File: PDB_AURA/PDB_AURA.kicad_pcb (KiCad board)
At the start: 4 copper layers, 50 x 50 mm, 84 parts, among them J100 XT30PW-M, J300 XT30PW-F, J301 XT30PW-F, J302 532617012, J303 XT30PW-F, J304 XT30PW-F, Q100 CSD18540Q5B, Q200 CSD18540Q5B, Q201 CSD18510Q5B, Q300 HSK10N06, Q301 HSK10N06, U100 LM74700, U200 LM25145RGYR, U300 LTV-217-B-G, U301 LTV-217-B-G, U302 INA219AIDCNR

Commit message: Continued Routing
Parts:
- C218: moved to F.Cu
- moved D300 29.0 mm to (60.5, 58.0)
- moved D301 29.0 mm to (89.5, 58.0)
- moved TP200 10.5 mm to (91.0, 79.0)
- moved C218 7.16 mm to (97.5, 62.5), turned to 90 degrees
- moved JP100 1.80 mm to (68.2, 79.0)
- moved R301 1.58 mm to (63.2, 65.0), turned to 180 degrees
- moved R307 1.58 mm to (86.8, 65.0), turned to 0 degrees
- moved TP201 0.15 mm to (70.0, 68.3)
- turned U300 to 90 degrees
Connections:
- J100 pad 4: GND -> +BATT
- J302 pad 1: +5V -> GND
- J302 pad 10: GND -> +5V
- J302 pad 11: GND -> +5V
- J302 pad 12: GND -> +5V
- J302 pad 2: +5V -> GND
- J302 pad 3: +5V -> GND
- J302 pad 5: SCL -> SDA
- J302 pad 6: SDA -> SCL
- J303 pad 3: GND -> +BATT_FILT
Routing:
- net GND: track 0.00 -> 21.4 mm, vias 162 -> 180
- net SDA: track 0.00 -> 19.5 mm
- net SCL: track 0.00 -> 19.2 mm
- net /200_Buck_Regulator/5V_HO: track 0.00 -> 19.1 mm, vias 0 -> 2
- net +5V_VCC: track 0.00 -> 17.8 mm, vias 0 -> 3
- net MSFT_2: track 0.00 -> 17.5 mm
- net /300_Connectors/VGS_CH1: track 0.00 -> 13.9 mm, vias 0 -> 2
- net /200_Buck_Regulator/COMP_FB_C: track 0.00 -> 13.5 mm, vias 0 -> 2
- net MSFT_1: track 0.00 -> 13.3 mm
- net /200_Buck_Regulator/5V_FB: track 0.00 -> 13.2 mm, vias 0 -> 1
- net /300_Connectors/MSFT_2_R: track 0.00 -> 13.0 mm, vias 0 -> 2
- net /300_Connectors/MSFT_1_R: track 0.00 -> 9.20 mm
- net /200_Buck_Regulator/5V_LO: track 0.00 -> 8.64 mm, vias 0 -> 2
- net /200_Buck_Regulator/5V_SW: track 0.00 -> 7.45 mm
- net +5V: track 0.00 -> 6.99 mm, vias 3 -> 5
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- added copper zone on B.Cu, net +5V
- added copper zone on B.Cu, net +BATT
- added copper zone on F.Cu, net +BATT
- added copper zone on In2.Cu, net +BATT_FILT
- added copper zone on F.Cu, net /300_Connectors/VBAT_CH1
- added copper zone on F.Cu, net /300_Connectors/VBAT_CH2
- added copper zone on B.Cu, net INA_IN+
- added copper zone on F.Cu, net INA_IN+

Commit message: First PDB Version
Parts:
- moved D200 2.03 mm to (96.5, 71.2)
- moved R211 2.03 mm to (93.9, 71.2)
- moved D100 1.75 mm to (96.5, 69.2)
- moved R101 1.72 mm to (93.9, 69.2)
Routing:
- net +5V: track 6.99 -> 72.5 mm, vias 5 -> 20
- net +3V3: track 0.00 -> 44.0 mm, vias 0 -> 2
- net MSFT_1: track 13.3 -> 47.0 mm, vias 0 -> 1
- net SCL: track 19.2 -> 38.2 mm, vias 0 -> 1
- net SDA: track 19.5 -> 37.0 mm, vias 0 -> 1
- net /300_Connectors/VGS_CH2: track 0.99 -> 14.4 mm
- net MSFT_2: track 17.5 -> 27.1 mm, vias 0 -> 1
- net /300_Connectors/VBAT_CH1: track 0.00 -> 6.71 mm, vias 2 -> 0
- net /200_Buck_Regulator/5V_SW: track 7.45 -> 13.6 mm, vias 12 -> 20
- net +BATT_FILT: track 5.73 -> 11.1 mm, vias 174 -> 181
- net GND: track 21.4 -> 23.9 mm, vias 180 -> 192
- net /200_Buck_Regulator/5V_HO: track 19.1 -> 20.3 mm
- net /200_Buck_Regulator/5V_LED: track 0.00 -> 1.28 mm
- net /100_Power/VBAT_LED: track 0.00 -> 1.28 mm
- net INA_IN+: vias 25 -> 33
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- added copper zone on B.Cu, net +BATT_FILT
- added copper zone on B.Cu, net /200_Buck_Regulator/5V_SW

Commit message: Second Iteration
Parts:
- C204, C205: value 22u -> 47u
- TP200, TP202: moved to F.Cu
- moved C205 13.4 mm to (89.5, 91.8)
- moved TP200 11.0 mm to (94.2, 89.5), turned to 0 degrees
- moved C216 3.50 mm to (95.5, 79.8)
- moved TP202 1.90 mm to (71.8, 74.2), turned to 0 degrees
- moved C210 1.00 mm to (74.8, 74.2)
- moved R210 1.00 mm to (75.8, 74.2)
- moved C300 0.50 mm to (73.3, 91.5)
- moved U302 0.50 mm to (75.8, 91.5)
- moved L200 0.25 mm to (85.2, 82.5), turned to -90 degrees
- moved TP203 0.10 mm to (70.0, 71.0)
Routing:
- net +5V: track 72.5 -> 83.1 mm, vias 20 -> 18
- net GND: track 23.9 -> 31.4 mm, vias 192 -> 253
- net +BATT: track 6.51 -> 0.00 mm, vias 49 -> 45
- net INA_IN+: track 3.58 -> 8.95 mm, vias 33 -> 38
- net +BATT_FILT: track 11.1 -> 14.2 mm, vias 181 -> 178
- net /200_Buck_Regulator/5V_PGOOD: track 4.44 -> 2.80 mm, vias 1 -> 0
- net /200_Buck_Regulator/5V_SW: track 13.6 -> 12.0 mm, vias 20 -> 9
- net MSFT_2: track 27.1 -> 28.6 mm
- net /300_Connectors/MSFT_2_R: track 13.0 -> 11.8 mm
- net SCL: track 38.2 -> 39.1 mm, vias 1 -> 3
- net SDA: track 37.0 -> 37.6 mm, vias 1 -> 3
- net /300_Connectors/VGS_CH2: track 14.4 -> 14.5 mm, vias 0 -> 2
- net +5V_VCC: track 17.8 -> 17.7 mm, vias 3 -> 2
- net +3V3: vias 2 -> 4

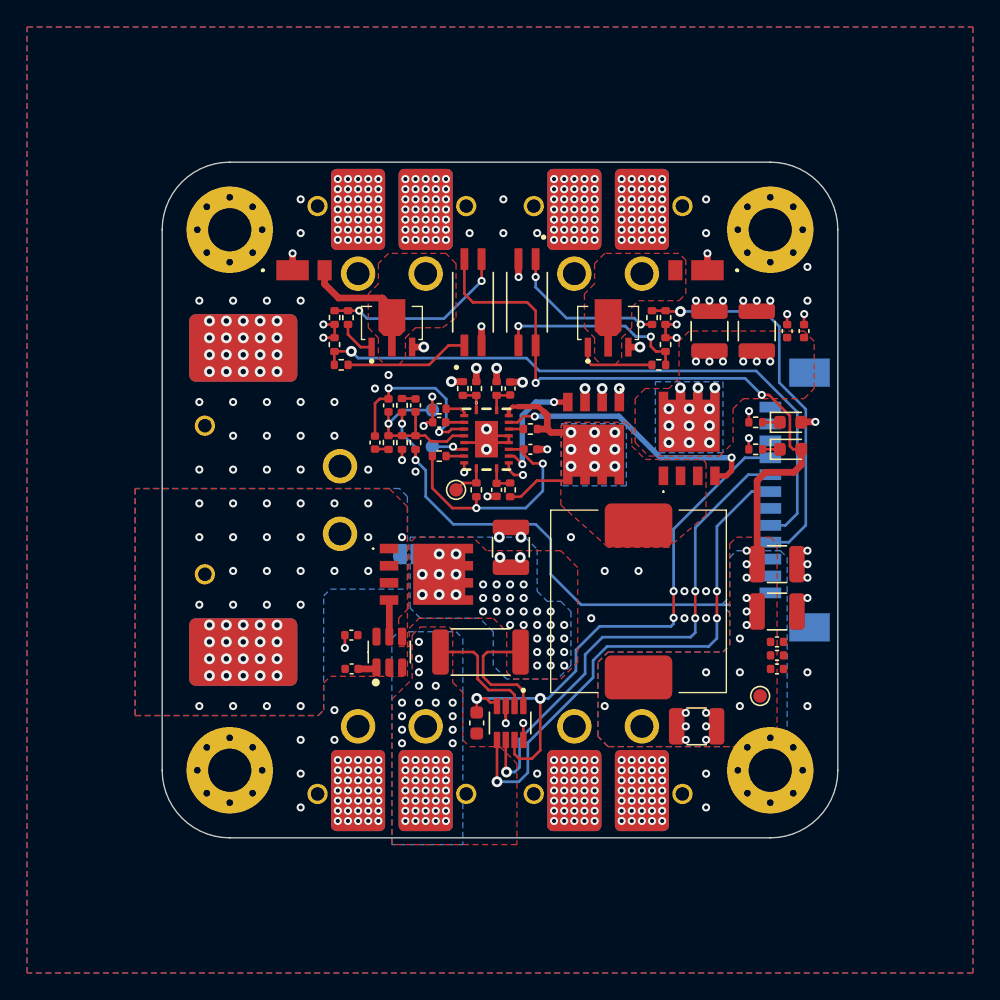
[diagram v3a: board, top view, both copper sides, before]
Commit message: Replaced JTAG with Flash
JTAG is used through USB so a Flash chip was added to MCU. PDB is just being cleaned up currently.
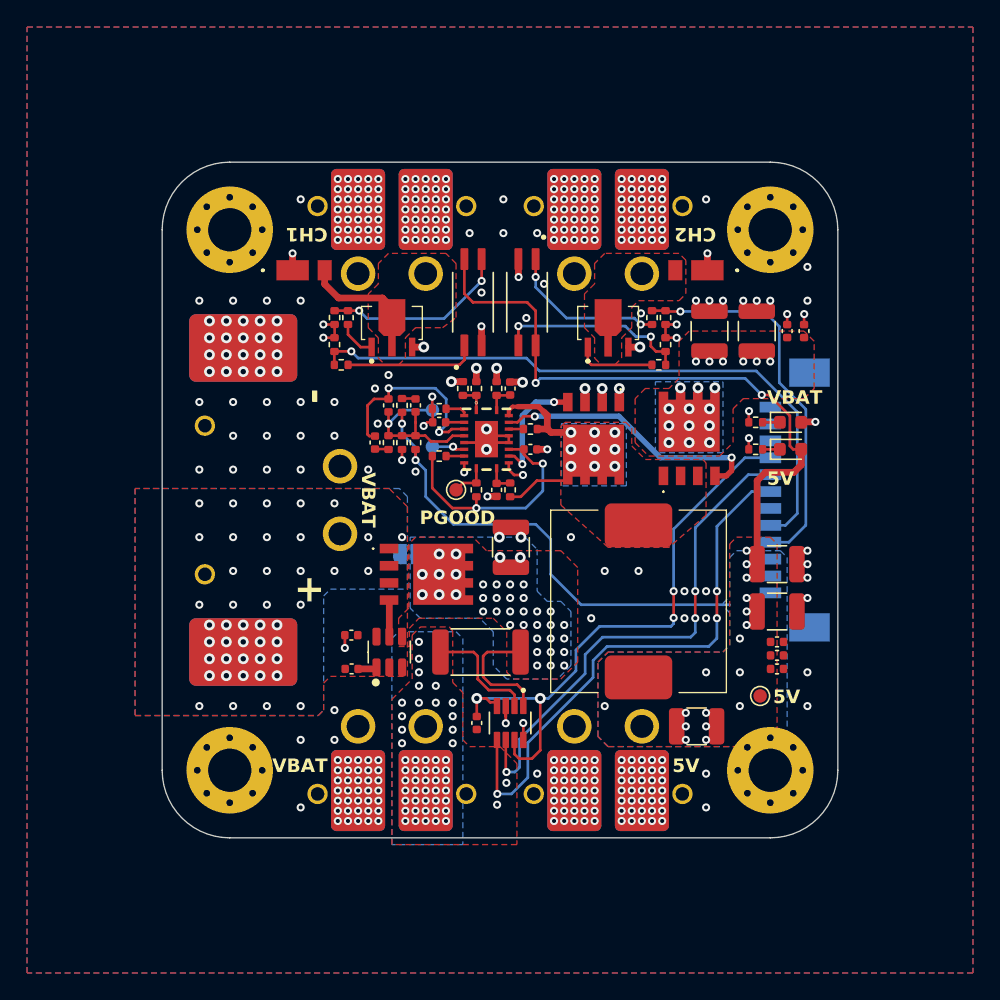
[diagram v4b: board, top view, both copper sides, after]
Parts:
- C300: footprint Capacitor_SMD:C_0603_1608Metric -> Capacitor_SMD:C_0402_1005Metric
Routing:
- net SCL: track 39.1 -> 40.6 mm
- net /200_Buck_Regulator/COMP_FB_C: track 13.5 -> 14.5 mm
- net /300_Connectors/MSFT_1_R: track 9.20 -> 9.83 mm
- net GND: vias 253 -> 257
- net +BATT: vias 45 -> 44
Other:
- board text added: "+"
- board text added: "-"
- board text added: "5V"
- board text added: "5V_FB"
- board text added: "CH1"
- board text added: "CH2"
- board text added: "PGOOD"
- board text added: "Power"
- board text added: "SYNC"
- board text added: "VBAT"

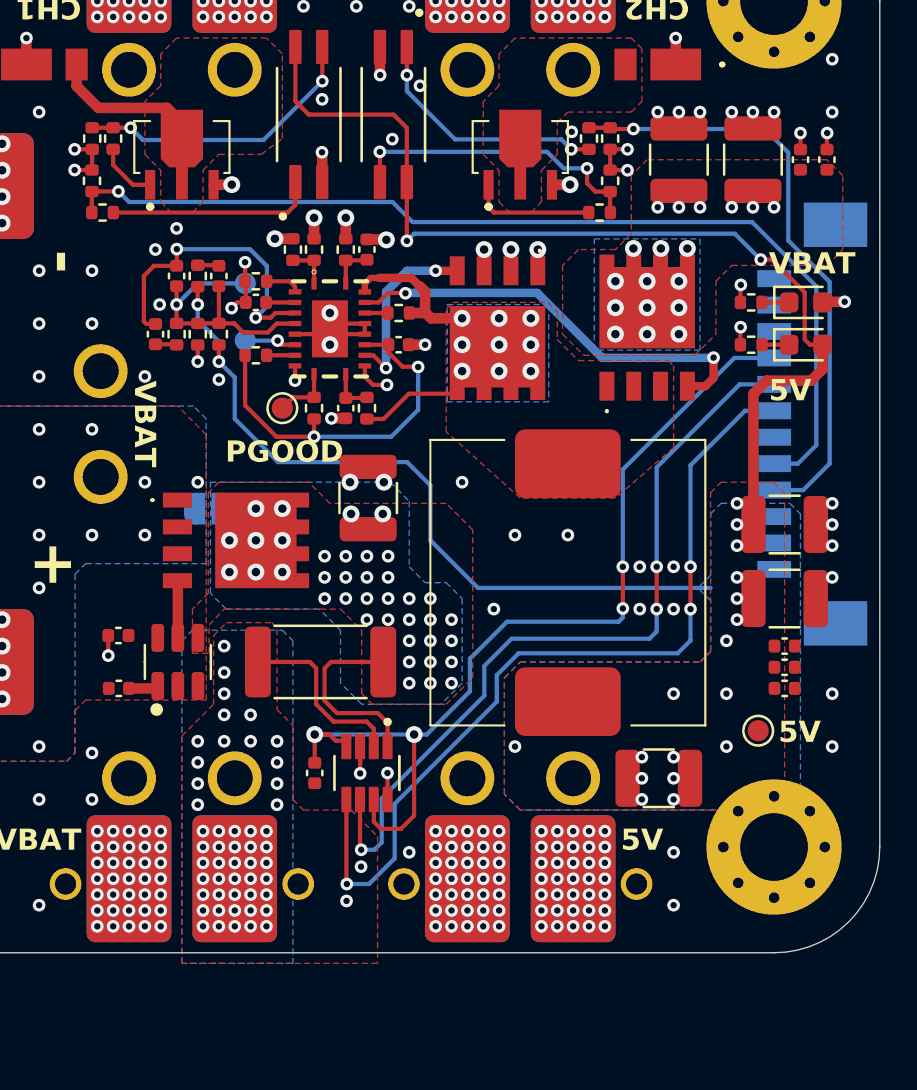
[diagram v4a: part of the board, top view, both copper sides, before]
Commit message: Fixed LM2514 Layout
Followed datasheet guidelines for the SW and HO traces.
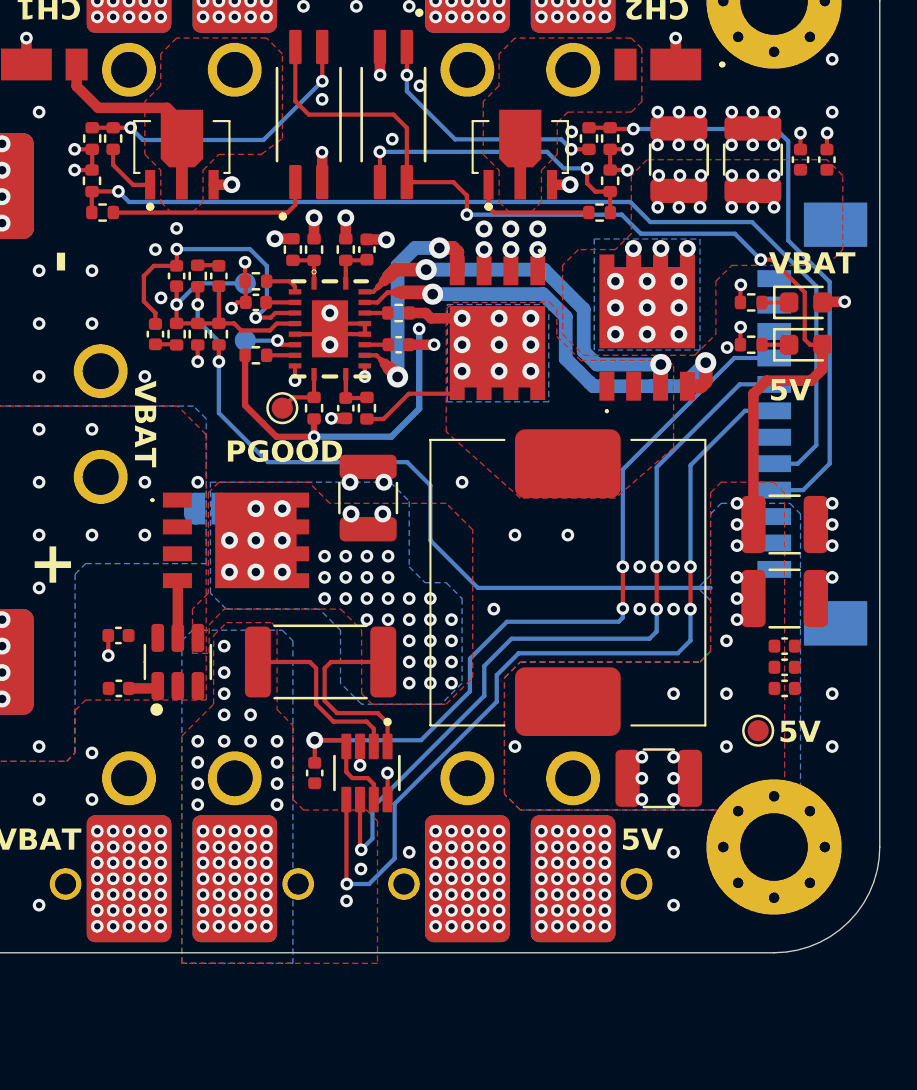
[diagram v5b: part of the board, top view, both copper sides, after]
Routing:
- net /200_Buck_Regulator/5V_SW: track 12.0 -> 26.0 mm, vias 9 -> 11
- net +3V3: track 44.0 -> 40.0 mm, vias 4 -> 3
- net /200_Buck_Regulator/5V_LO: track 8.63 -> 11.4 mm
- net /200_Buck_Regulator/5V_HO: track 20.3 -> 21.6 mm
- net +5V: track 83.1 -> 82.0 mm
- net GND: track 31.4 -> 30.4 mm, vias 257 -> 266
- net +BATT_FILT: vias 178 -> 184

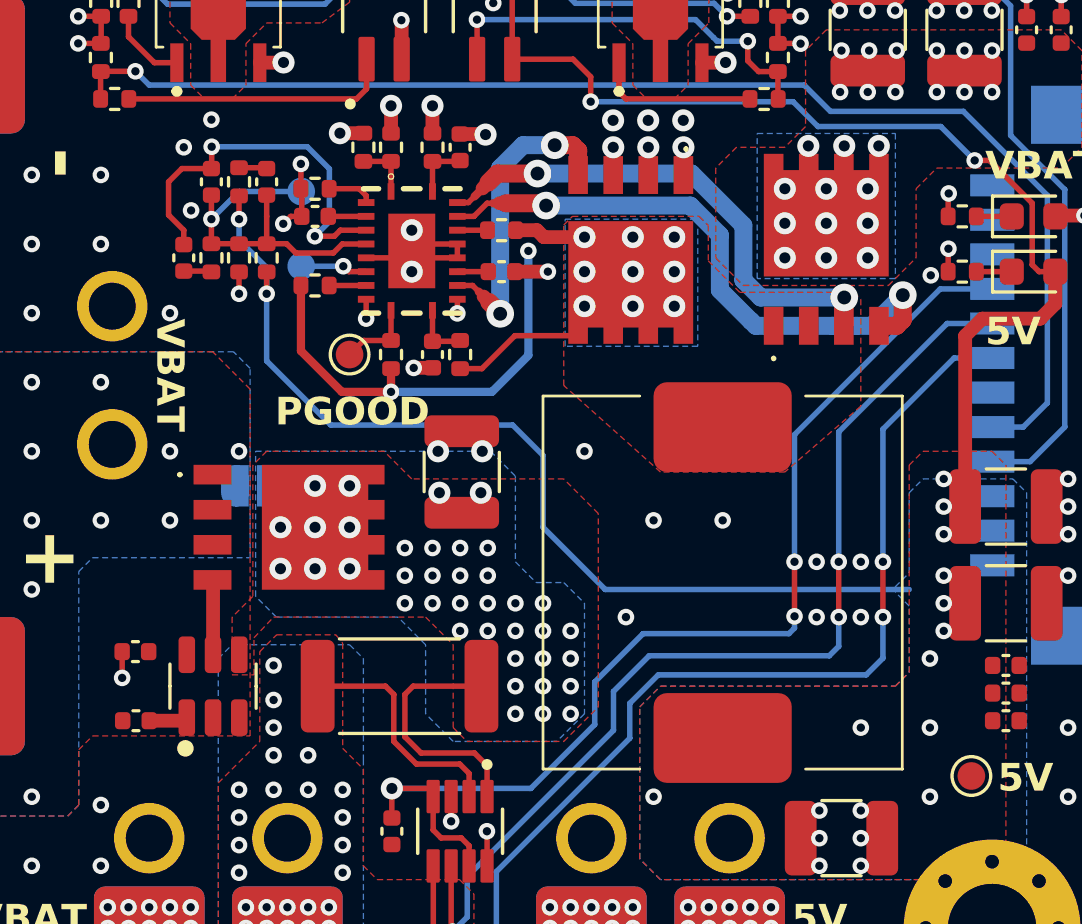
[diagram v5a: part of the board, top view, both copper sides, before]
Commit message: New Component Values
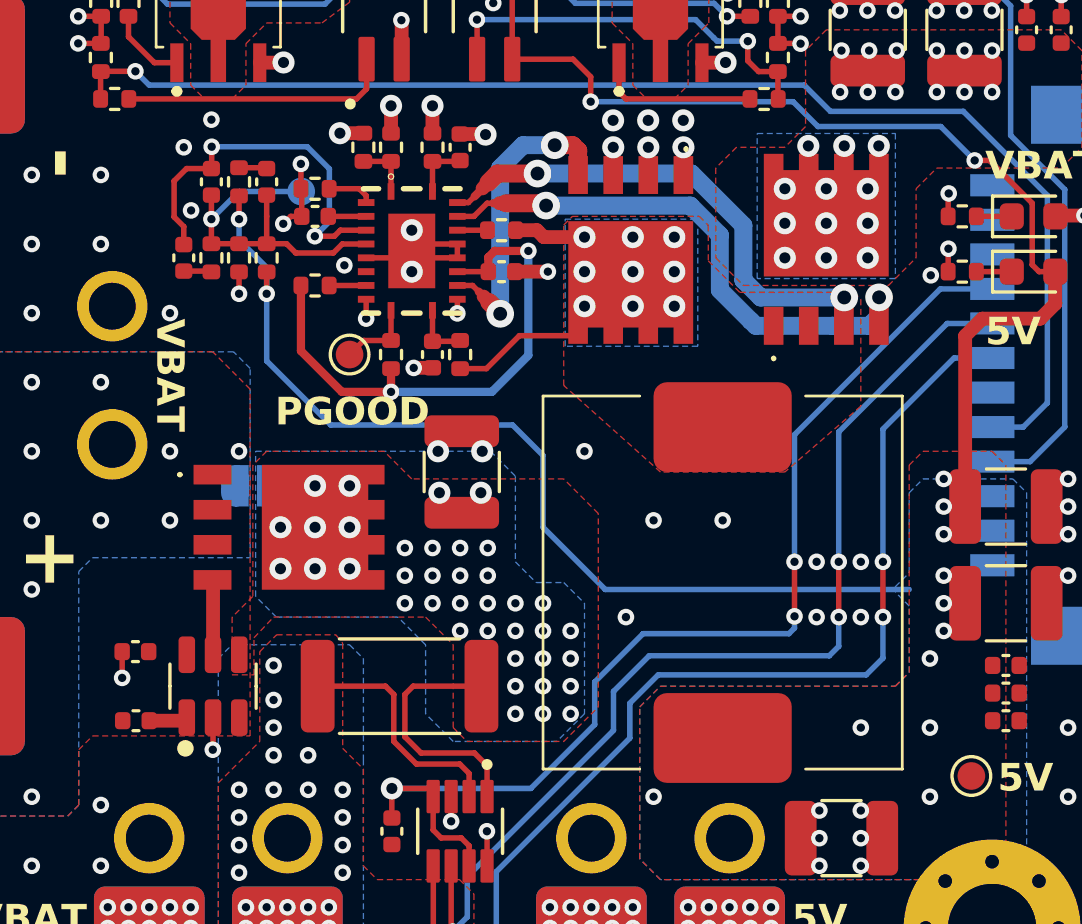
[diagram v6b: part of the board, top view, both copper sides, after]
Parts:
- removed TP203: TestPoint, TestPoint:TestPoint_Pad_D1.0mm
- C210: value 10p -> 27p
- C211: value 100n -> 47n
- C212: value 1n -> 2n2
- C213: value 8n2 -> 18n
- C214: value 390p -> 1n8
- R200: value 2R1 -> 0R
- R201: value 35k7 -> 39k
- R202: value 9k1 -> 10k
- R203: value 20k -> 10k
- R204: value 249R -> 22R
- R205: value 3k4 -> 1k
- R206: value 18k -> 5k1
- R207: value 1k47 -> 680R
- R208: value 4k7 -> 39k
- R209: value 4k7 -> 10k
- R210: value 576R -> 220R
- R211: value 4k7 -> 1k
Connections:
- U200 pad 7: /200_Buck_Regulator/5V_SYNCOUT -> unconnected-(U200-SYNCOUT-Pad7)
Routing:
- net /200_Buck_Regulator/5V_SYNCOUT: track 2.44 -> 0.00 mm, vias 1 -> 0
- net /200_Buck_Regulator/5V_HO: track 21.6 -> 19.3 mm
- net +5V_VCC: track 17.5 -> 19.6 mm
- net GND: track 30.4 -> 31.6 mm, vias 266 -> 268
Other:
- board text removed: "SYNC"
